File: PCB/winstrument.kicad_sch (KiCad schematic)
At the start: 14 parts, among them J1 Conn_01x05_Pin, J2 Conn_01x06_Pin, U1 STM32L432KCUx, U2 TCAN337, U3 SN74AVC4T245PW, U4 ADM3488ExR, U5 SN74AVC4T245PW, U6 LM2594HVM-3.3, U7 LM2594M-5.0, U8 LM2594N-12

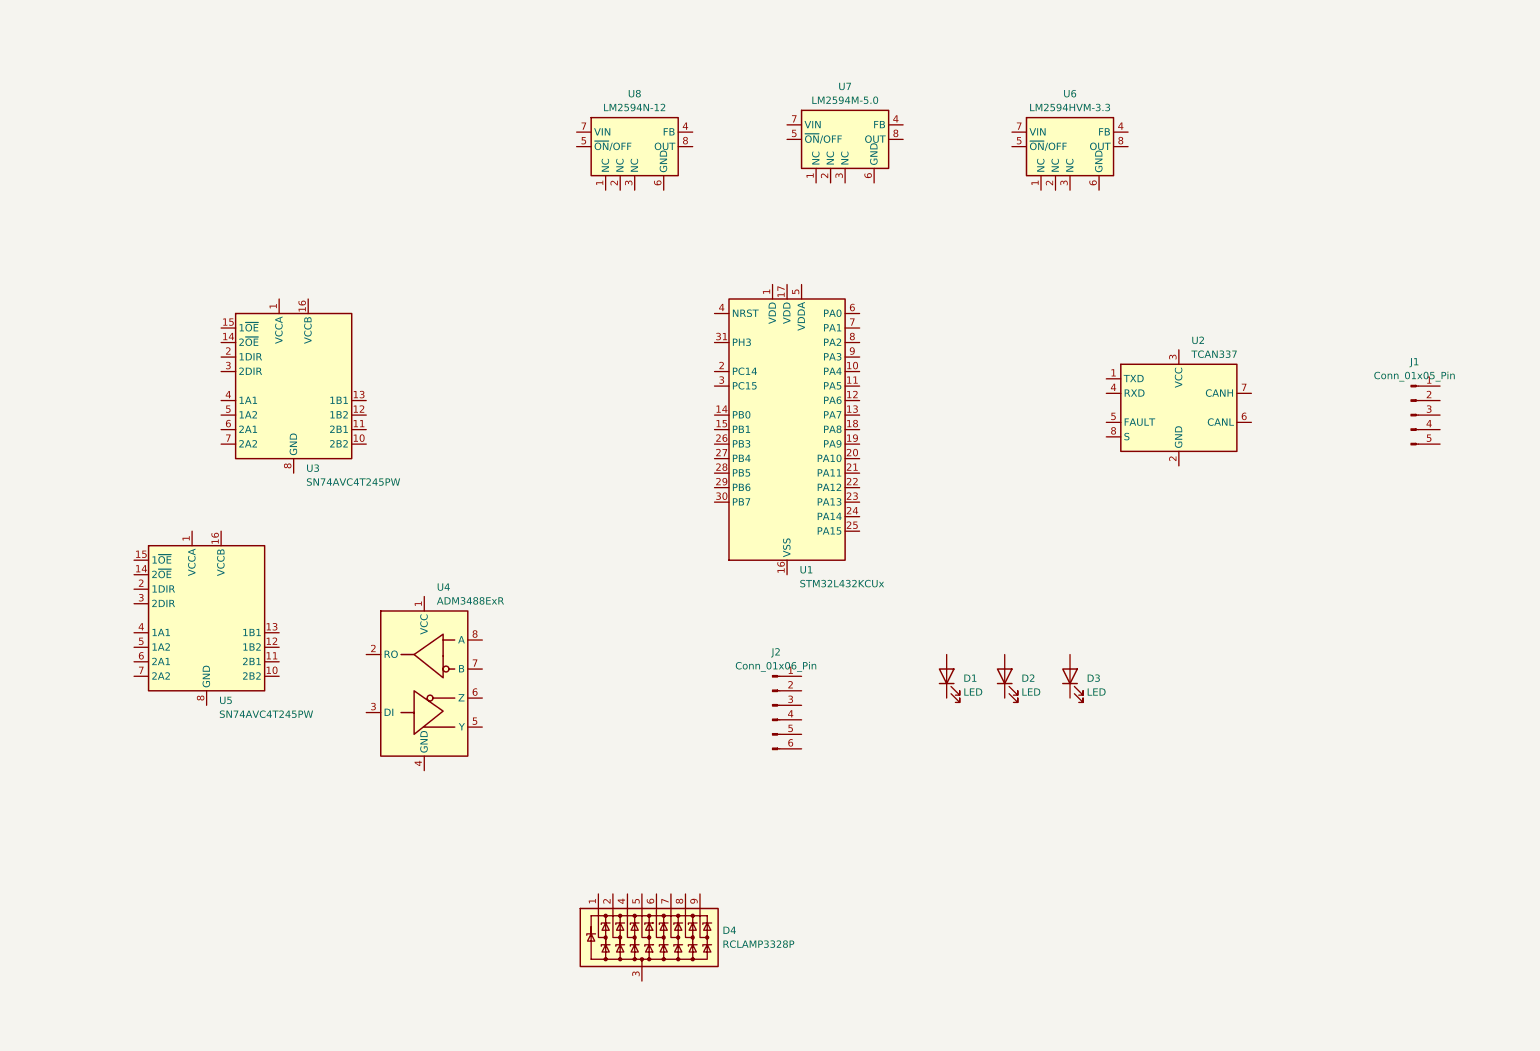
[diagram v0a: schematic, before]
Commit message: begin PCB schemaitic layout for a universal instrument interface
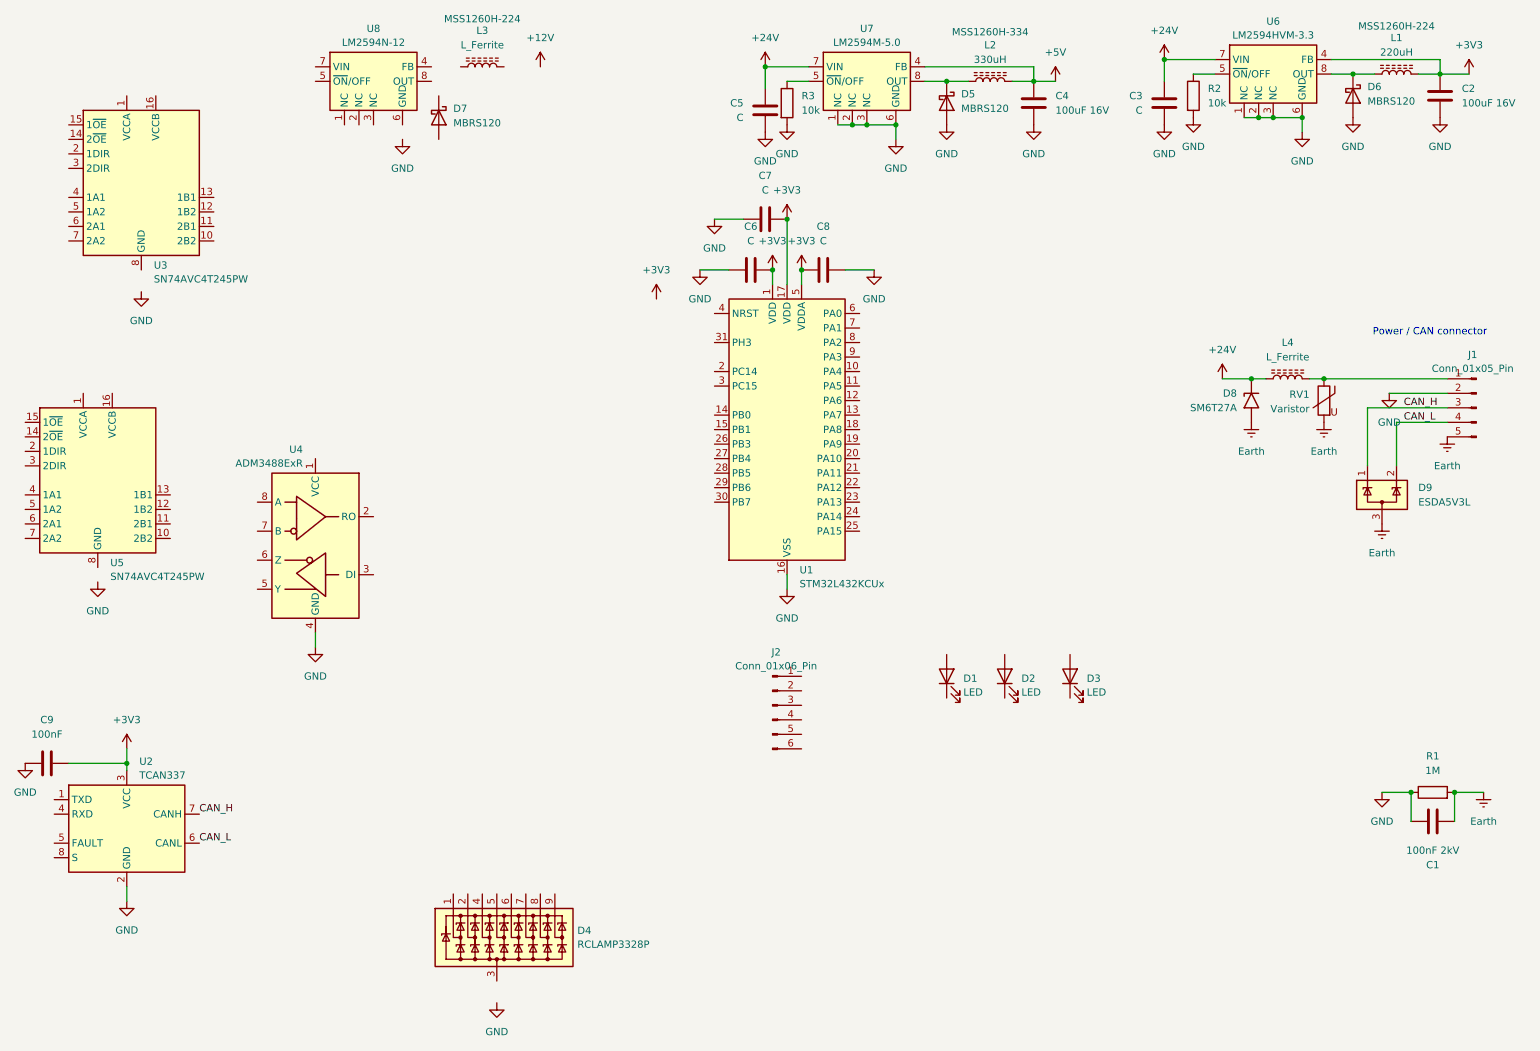
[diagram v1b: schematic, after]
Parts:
- added C1: 100nF 2kV, symbol Device:C
- added C2, C4: 100uF 16V, symbol Device:C
- added C3, C5, C6, C7, C8: C, symbol Device:C
- added C9: 100nF, symbol Device:C
- added D5, D6, D7: MBRS120, Diode_SMD:D_SMB_Handsoldering, symbol Device:D_Schottky
- added D8: SM6T27A, Diode_SMD:D_SMB, symbol Diode:SM6T27A
- added D9: ESDA5V3L, Package_TO_SOT_SMD:SOT-23-3, symbol Power_Protection:ESDA5V3L
- added L1: 220uH, symbol Device:L_Ferrite
- added L2: 330uH, symbol Device:L_Ferrite
- added L3, L4: L_Ferrite, symbol Device:L_Ferrite
- added R1: 1M, symbol Device:R
- added R2, R3: 10k, symbol Device:R
- added RV1: Varistor, symbol Device:Varistor
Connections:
- net GND: now reaches U7.1 (NC)
- net GND: now also J1.2 (Pin_2), U1.16 (VSS), U1.32 (VSS), U1.33 (VSS), U2.2 (GND), U4.4 (GND), U6.1 (NC), U6.2 (NC), U6.3 (NC), U6.6 (GND), U7.2 (NC), U7.3 (NC), U7.6 (GND), C1.1, C2.2, C3.2, C4.2, C5.2, C6.1, C7.1, C8.2, C9.1, D5.2 (A), D6.2 (A), R1.1, R2.2, R3.2
- net +5V: now reaches U7.4 (FB)
- net +5V: now also C4.1, L2.2
- net at U7.5 (~{ON}/OFF): now also R3.1
- net +24V: now reaches U7.7 (VIN)
- net +24V: now also U6.7 (VIN), C3.1, C5.1, D8.1 (A1), L4.1
- net at U7.8 (OUT): now also D5.1 (K), L2.1
- net +3V3: now reaches U2.3 (VCC)
- net +3V3: now also U1.1 (VDD), U1.17 (VDD), U1.5 (VDDA), U6.4 (FB), C2.1, C6.2, C7.2, C8.1, C9.2, L1.2
- net CAN_L: now reaches U2.6 (CANL)
- net CAN_L: now also J1.4 (Pin_4), D9.2 (K)
- net CAN_H: now reaches U2.7 (CANH)
- net CAN_H: now also J1.3 (Pin_3), D9.1 (K)
- net at J1.1 (Pin_1): now also L4.2, RV1.1
- net Earth: now reaches J1.5 (Pin_5)
- net Earth: now also C1.2, D8.2 (A2), D9.3 (A), R1.2, RV1.2
- net at U6.5 (~{ON}/OFF): now also R2.1
- net at U6.8 (OUT): now also D6.1 (K), L1.1
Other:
- note added: "Power / CAN connector"
- moved on the sheet: D4, J1, U2, U3, U4, U5, U6, U7, U8

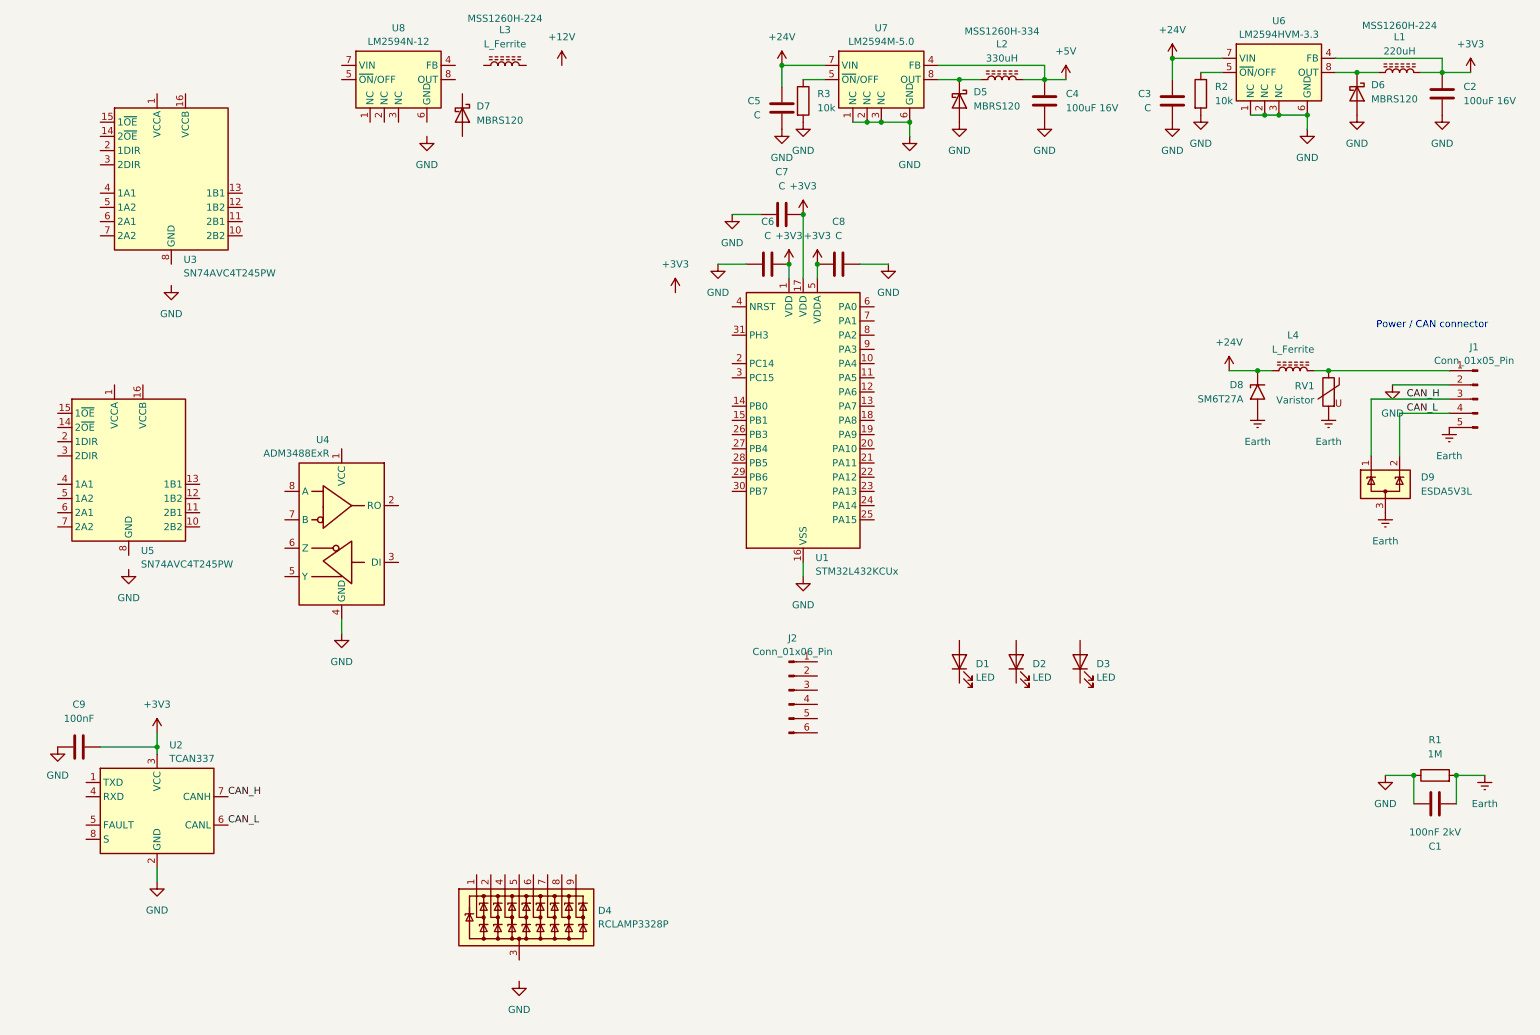
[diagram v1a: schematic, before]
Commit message: modification of the knowledgebase to fold in other work that had been accidentally duplicated.  Small progress on the schematic, evaluating using a digital isolator instead of an optoisolator for offboard serial communications.
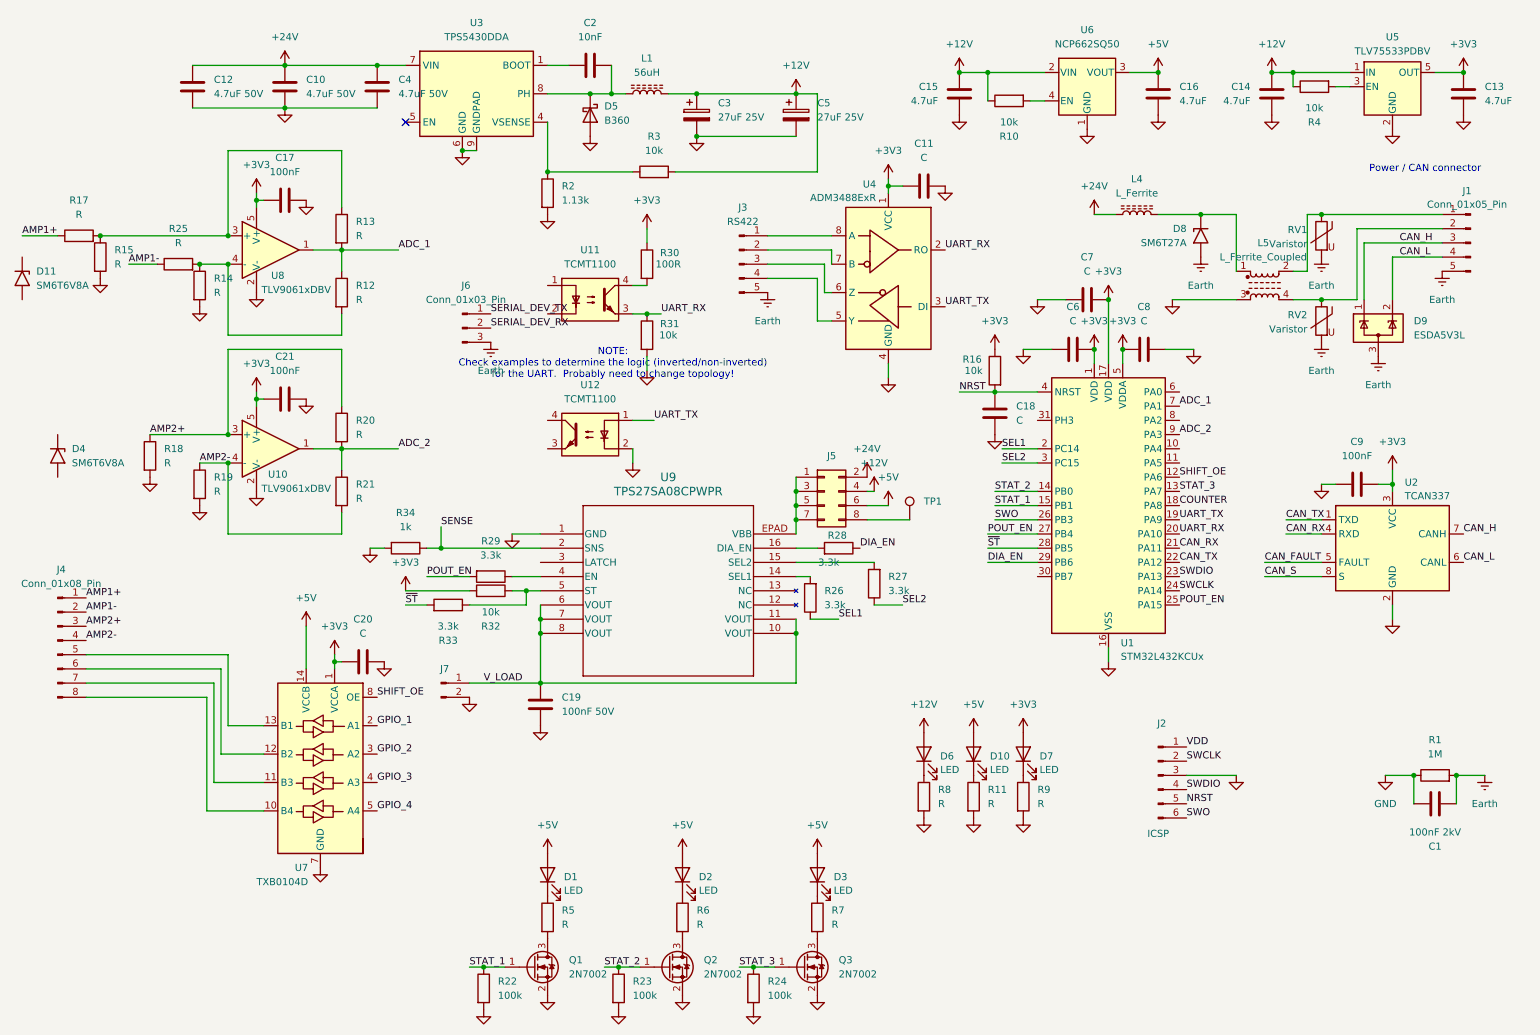
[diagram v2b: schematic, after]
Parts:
- removed C3, C5: C, symbol Device:C
- removed D4: RCLAMP3328P, Package_DFN_QFN:UDFN-9_1.0x3.8mm_P0.5mm, symbol Power_Protection:RCLAMP3328P
- removed D5, D6, D7: MBRS120, Diode_SMD:D_SMB_Handsoldering, symbol Device:D_Schottky
- removed L2: 330uH, symbol Device:L_Ferrite
- removed L3: L_Ferrite, symbol Device:L_Ferrite
- removed U3, U5: SN74AVC4T245PW, Package_SO:TSSOP-16_4.4x5mm_P0.65mm, symbol Logic_LevelTranslator:SN74AVC4T245PW
- removed U6: LM2594HVM-3.3, Package_SO:SOIC-8_3.9x4.9mm_P1.27mm, symbol Regulator_Switching:LM2594HVM-3.3
- removed U7: LM2594M-5.0, Package_SO:SOIC-8_3.9x4.9mm_P1.27mm, symbol Regulator_Switching:LM2594M-5.0
- removed U8: LM2594N-12, Package_DIP:DIP-8_W7.62mm, symbol Regulator_Switching:LM2594N-12
- added C10, C12: 4.7uF 50V, symbol Device:C
- added C11, C18, C20: C, symbol Device:C
- added C13, C14, C15, C16: 4.7uF, symbol Device:C
- added C17, C21: 100nF, symbol Device:C
- added C19: 100nF 50V, symbol Device:C
- added C3, C5: 27uF 25V, symbol Device:C_Polarized
- added D10, D6, D7: LED, symbol Device:LED
- added D11, D4: SM6T6V8A, Diode_SMD:D_SMB, symbol Diode:SM6T6V8A
- added D5: B360, Diode_SMD:D_SMC, symbol Diode:B360
- added J3: RS422, symbol Connector:Conn_01x05_Pin
- added J4: Conn_01x08_Pin, symbol Connector:Conn_01x08_Pin
- added J5: Conn_02x04_Odd_Even, symbol Connector_Generic:Conn_02x04_Odd_Even
- added J6: Conn_01x03_Pin, symbol Connector:Conn_01x03_Pin
- added J7: Conn_01x02_Pin, symbol Connector:Conn_01x02_Pin
- added L5: L_Ferrite_Coupled, symbol Device:L_Ferrite_Coupled
- added Q1, Q2, Q3: 2N7002, Package_TO_SOT_SMD:SOT-23, symbol Transistor_FET:2N7002
- added R10, R16, R31, R32, R4: 10k, symbol Device:R
- added R11, R12, R13, R14, R15, R17, R18, R19, R20, R21, R25, R5, R6, R7, R8, R9: R, symbol Device:R
- added R22, R23, R24: 100k, symbol Device:R
- added R26, R27, R28, R29, R33: 3.3k, symbol Device:R
- added R30: 100R, symbol Device:R
- added R34: 1k, symbol Device:R
- added RV2: Varistor, symbol Device:Varistor
- added TP1: TestPoint, symbol Connector:TestPoint
- added U10, U8: TLV9061xDBV, Package_TO_SOT_SMD:SOT-23-5, symbol Amplifier_Operational:TLV9061xDBV
- added U11, U12: TCMT1100, Package_SO:SOP-4_4.4x2.6mm_P1.27mm, symbol Isolator:TCMT1100
- added U3: TPS5430DDA, Package_SO:TI_SO-PowerPAD-8_ThermalVias, symbol Regulator_Switching:TPS5430DDA
- added U5: TLV75533PDBV, Package_TO_SOT_SMD:SOT-23-5, symbol Regulator_Linear:TLV75533PDBV
- added U6: NCP662SQ50, Package_TO_SOT_SMD:SC-82AB, symbol Regulator_Linear:NCP662SQ50
- added U7: TXB0104D, Package_SO:SOIC-14_3.9x8.7mm_P1.27mm, symbol Logic_LevelTranslator:TXB0104D
- added U9: TPS27SA08CPWPR, TSSOP_CPWPR_TEX, symbol 2024-08-14_10-37-53:TPS27SA08CPWPR
- C1: footprint (none) -> Capacitor_SMD:C_1812_4532Metric
- C2: value 100uF 16V -> 10nF
- C4: value 100uF 16V -> 4.7uF 50V
- J2: value Conn_01x06_Pin -> ICSP
- L1: value 220uH -> 56uH; Part Number MSS1260H-224 -> (none)
- R1: footprint (none) -> Resistor_SMD:R_1206_3216Metric
- R2: value 10k -> 1.13k
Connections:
- net +12V: now also L1.2, R3.2, C14.1, C15.1, C3.1, C5.1, D6.2 (A), J5.4 (Pin_4), R10.1, R4.1, U5.1 (IN), U6.2 (VIN)
- net +24V: now also C4.1, C10.1, C12.1, J5.2 (Pin_2), U3.7 (VIN); no longer D8.1 (A1)
- net +3V3: now also U4.1 (VCC), C11.1, C13.1, C17.1, C20.1, C21.1, D7.2 (A), R16.1, R30.1, R32.2, U10.5 (V+), U5.5 (OUT), U7.1 (VCCA), U8.5 (V+); no longer C2.1, L1.2
- net +5V: now also D1.2 (A), D2.2 (A), D3.2 (A), C16.1, D10.2 (A), J5.6 (Pin_6), U6.3 (VOUT), U7.14 (VCCB); no longer C4.1
- net Earth: now also J3.5 (Pin_5), J6.3 (Pin_3), RV2.2
- net GND: now also J2.3 (Pin_3), C10.2, C11.2, C12.2, C13.2, C14.2, C15.2, C16.2, C17.2, C18.1, C19.1, C20.2, C21.2, C3.2, C5.2, D5.2 (A), J7.2 (Pin_2), L5.3, Q1.2 (S), Q2.2 (S), Q3.2 (S), R11.2, R14.2, R15.2, R18.2, R19.2, R22.2, R23.2, R24.2, R31.2, R34.2, R8.2, R9.2, U10.2 (V-), U12.2, U3.6 (GND), U3.9 (GNDPAD), U5.2 (GND), U6.1 (GND), U7.7 (GND), U8.2 (V-), U9.1 (GND); no longer C2.2, J1.2 (Pin_2), R3.2
- net at R3.1: now also R2.1, U3.4 (VSENSE)
- net at L1.1: now also C2.2, D5.1 (K), U3.8 (PH)
- net at D2.1 (K): now also R6.1
- net CAN_TX: now reaches U2.1 (TXD)
- net CAN_TX: now also U1.22 (PA12)
- net CAN_RX: now reaches U2.4 (RXD)
- net CAN_RX: now also U1.21 (PA11)
- net CAN_FAULT: now reaches U2.5 (FAULT)
- net CAN_S: now reaches U2.8 (S)
- net SHIFT_OE: now reaches U1.12 (PA6)
- net SHIFT_OE: now also U7.8 (OE)
- net STAT_3: now reaches U1.13 (PA7)
- net STAT_3: now also Q3.1 (G), R24.1
- net STAT_2: now reaches U1.14 (PB0)
- net STAT_2: now also Q2.1 (G), R23.1
- net STAT_1: now reaches U1.15 (PB1)
- net STAT_1: now also Q1.1 (G), R22.1
- net COUNTER: now reaches U1.18 (PA8)
- net UART_TX: now reaches U1.19 (PA9)
- net UART_TX: now also U4.3 (DI), U12.1
- net SEL1: now reaches U1.2 (PC14)
- net SEL1: now also R26.1
- net UART_RX: now reaches U1.20 (PA10)
- net UART_RX: now also U4.2 (RO), R31.1, U11.3
- net SWDIO: now reaches U1.23 (PA13)
- net SWDIO: now also J2.4 (Pin_4)
- net SWCLK: now reaches U1.24 (PA14)
- net SWCLK: now also J2.2 (Pin_2)
- net POUT_EN: now reaches U1.25 (PA15)
- net POUT_EN: now also U1.27 (PB4), R29.2
- net SWO: now reaches U1.26 (PB3)
- net SWO: now also J2.6 (Pin_6)
- net ~{ST}: now reaches U1.28 (PB5)
- net ~{ST}: now also R33.2
- net DIA_EN: now reaches U1.29 (PB6)
- net DIA_EN: now also R28.1
- net SEL2: now reaches U1.3 (PC15)
- net SEL2: now also R27.1
- net NRST: now reaches U1.4 (NRST)
- net NRST: now also J2.5 (Pin_5), C18.2, R16.2
- net ADC_1: now reaches U1.7 (PA1)
- net ADC_1: now also R12.1, R13.2, U8.1
- net ADC_2: now reaches U1.9 (PA3)
- net ADC_2: now also R20.2, R21.1, U10.1
- net at D3.1 (K): now also R7.1
- net at J1.1 (Pin_1), RV1.1: now also L5.2; no longer L4.2
- net at D1.1 (K): now also R5.1
- net VDD: now reaches J2.1 (Pin_1)
- net at U4.5 (Y): now also J3.4 (Pin_4)
- net at U4.6 (Z): now also J3.3 (Pin_3)
- net at U4.7 (B): now also J3.2 (Pin_2)
- net at U4.8 (A): now also J3.1 (Pin_1)
- new net: D6.1 (K), R8.1
- new net: R10.2, U6.4 (EN)
- new net: R12.2, R14.1, R25.2, U8.4 (-)
- new net: J4.5 (Pin_5), U7.13 (B1)
- new net: J4.6 (Pin_6), U7.12 (B2)
- new net: J4.7 (Pin_7), U7.11 (B3)
- new net: J4.8 (Pin_8), U7.10 (B4)
- new net: R30.2, U11.4
- new net: C2.1, U3.1 (BOOT)
- new net: Q1.3 (D), R5.2
- new net: Q3.3 (D), R7.2
- new net: J1.2 (Pin_2), L5.4, RV2.1
- new net: R4.2, U5.3 (EN)
- new net: R29.1, U9.4 (EN)
- new net: D10.1 (K), R11.1
- new net: R26.2, U9.14 (SEL1)
- new net: R27.2, U9.15 (SEL2)
- new net: R28.2, U9.16 (DIA_EN)
- new net: R32.1, R33.1, U9.5 (ST)
- new net: J5.1 (Pin_1), J5.3 (Pin_3), J5.5 (Pin_5), J5.7 (Pin_7), U9.EPAD (VBB)
- new net: D8.1 (A1), L4.2, L5.1
- new net: R13.1, R15.1, R17.2, U8.3 (+)
- new net: D7.1 (K), R9.1
- new net: J5.8 (Pin_8), TP1.1
- new net: Q2.3 (D), R6.2
- new net AMP1+: J4.1 (Pin_1), R17.1
- new net AMP1-: J4.2 (Pin_2), R25.1
- new net AMP2+: J4.3 (Pin_3), R18.1, R20.1, U10.3 (+)
- new net AMP2-: J4.4 (Pin_4), R19.1, R21.2, U10.4 (-)
- new net GPIO_1: U7.2 (A1)
- new net GPIO_2: U7.3 (A2)
- new net GPIO_3: U7.4 (A3)
- new net GPIO_4: U7.5 (A4)
- new net SENSE: R34.1, U9.2 (SNS)
- new net SERIAL_DEV_RX: J6.2 (Pin_2)
- new net SERIAL_DEV_TX: J6.1 (Pin_1)
- new net V_LOAD: C19.2, J7.1 (Pin_1), U9.10 (VOUT), U9.11 (VOUT), U9.6 (VOUT), U9.7 (VOUT), U9.8 (VOUT)
- no-connect marks 0 -> 1
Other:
- note added: "NOTE: Check examples to determine the logic (inverted/non-inverted) for the UART. Probably need to change topology!"
- moved on the sheet: C6, C7, C8, C9, D1, D2, D3, D8, D9, J1, J2, RV1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
